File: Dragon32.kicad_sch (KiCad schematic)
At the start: 67 parts, among them IC1 74LS273N, IC11 74LS123N, IC12 LM1889N, IC13 2318, IC15 MC14053, IC2 MC6847, J1 Board Interconnect Male, J2 Video Output, J3 JTAG, U1 ATF1504ASL-xAx44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

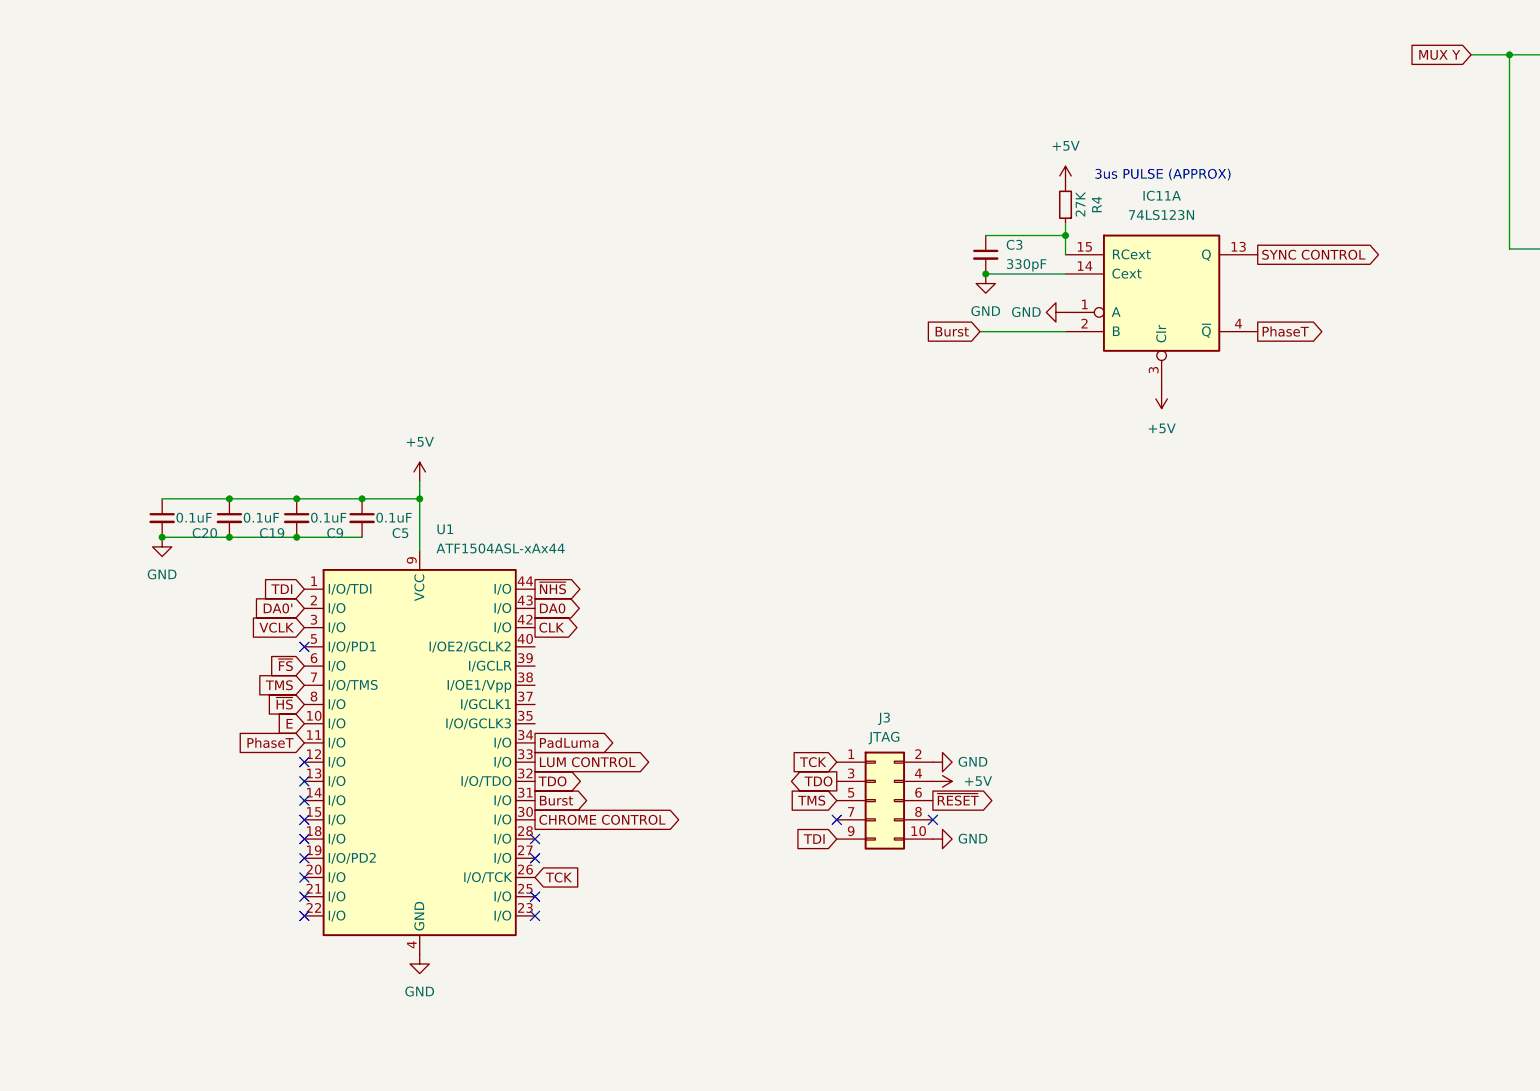
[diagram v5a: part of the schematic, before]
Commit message: convert to KiCad 8
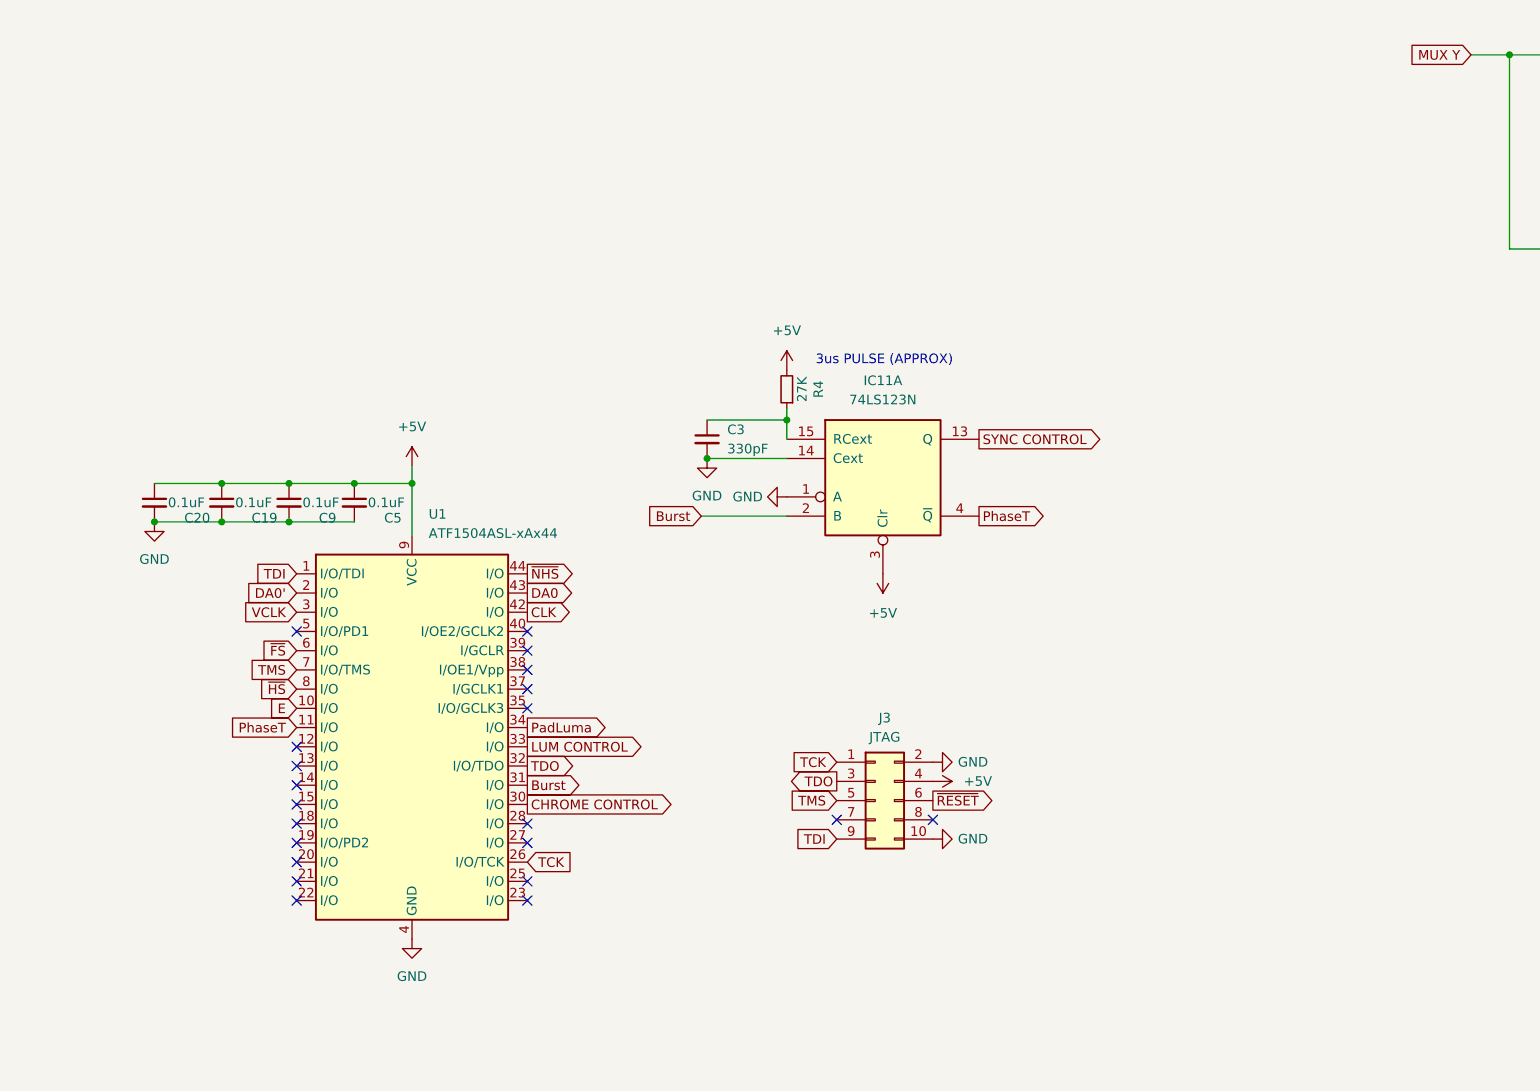
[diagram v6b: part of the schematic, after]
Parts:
- U1: DigiKey (none) -> ATF1504ASL-25AU44-ND
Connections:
- no-connect marks 44 -> 49
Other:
- moved on the sheet: C19, C20, C3, C5, C9, IC11A, R4, U1
